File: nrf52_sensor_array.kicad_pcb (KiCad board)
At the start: 2 copper layers, 52.4 x 33.1 mm, 61 parts, among them J1 CONN_01X08, J2 CONN_01X08, J3 CONN_01X08, J4 CONN_01X08, J5 CONN_01X08, J6 CONN_01X08, P1 CONN_2, P2 CONN_2, P3 CONN_2, P4 CONN_2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

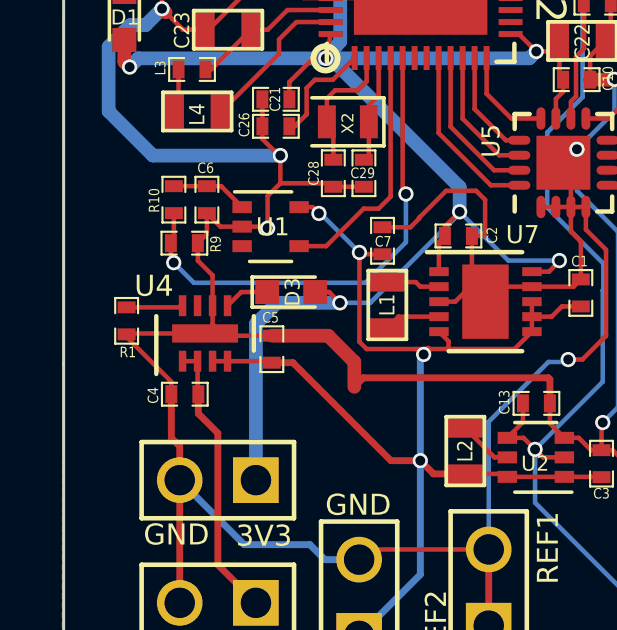
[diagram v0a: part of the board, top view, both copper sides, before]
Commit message: Placed corrected footprint.
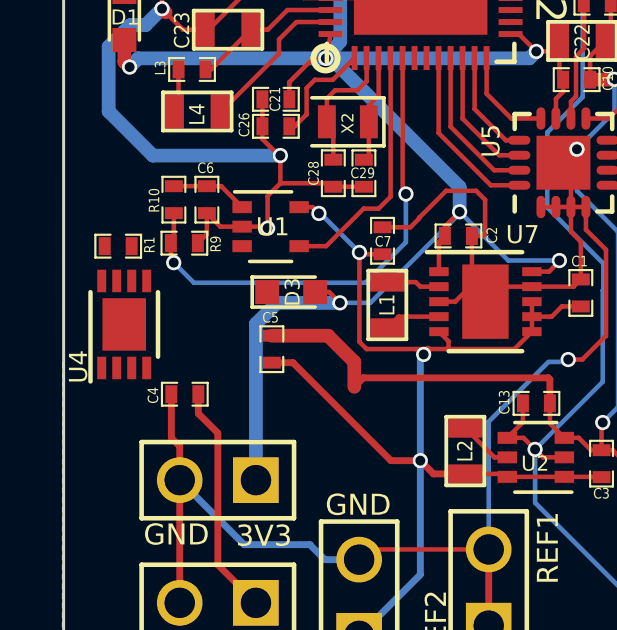
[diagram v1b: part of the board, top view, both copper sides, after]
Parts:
- U4: footprint Housings_DFN_QFN:DFN-8-1EP_2x3mm_Pitch0.5mm -> Housings_DFN_QFN:DFN-8-1EP_3x2mm_Pitch0.5mm
- moved U4 2.71 mm to (267.9, 145.9)
- moved R1 2.51 mm to (267.7, 143.3), turned to 180 degrees
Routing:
- net AVSS: track 254.0 -> 243.1 mm
- net VCC: track 41.3 -> 39.4 mm
- net Net-(R1-Pad2): track 1.92 -> 0.00 mm
- net 5V_in_charge: track 9.36 -> 7.79 mm
- net Net-(D3-Pad1): track 1.51 -> 0.00 mm

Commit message: (work in progress), missing ground connection on PCB, no load sharing circuit.
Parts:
- moved C4 1.10 mm to (270.2, 149.3)
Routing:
- net AVSS: track 243.1 -> 249.8 mm, vias 17 -> 18
- net VCC: track 39.4 -> 44.1 mm
- net Net-(D3-Pad1): track 0.00 -> 4.17 mm
- net 5V_in_charge: track 7.79 -> 11.4 mm
- net Net-(R1-Pad2): track 0.00 -> 1.20 mm
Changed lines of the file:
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@@
   (general
     (links 238)
-    (no_connects 13)
-    (area 265.849999 125.449999 318.320001 158.600001)
+    (no_connects 0)
+    (area 265.6476 122.157123 321.400001 159.215733)
     (thickness 1.6)
     (drawings 27)
-    (tracks 1155)
+    (tracks 1177)
     (zones 0)
     (modules 61)
@@
   )
   (setup
-    (last_trace_width 0.4572)
+    (last_trace_width 0.229)
     (user_trace_width 0.152)
     (user_trace_width 0.229)
@@
   )
   (module SM0402 (layer F.Cu)
-    (at 269.94 148.205)
+    (at 270.24 149.26)
     (attr smd)
     (fp_text reference C4 (at -1.05 0.04 90) (layer F.SilkS)
@@
   (segment (start 269.73042 137.38) (end 269.73042 138.64258) (width 0.152) (layer F.Cu) (net 8))
   (segment (start 269.73042 138.64258) (end 269.593 138.78) (width 0.152) (layer F.Cu) (net 8))
+  (segment (start 269.77 151.07) (end 269.77 149.28042) (width 0.152) (layer F.Cu) (net 9))
+  (segment (start 269.77 149.28042) (end 269.79042 149.26) (width 0.152) (layer F.Cu) (net 9))
+  (segment (start 273.125 140.25) (end 268.875 140.25) (width 0.152) (layer B.Cu) (net 9))
+  (via (at 268.875 140.25) (size 0.508) (drill 0.3302) (layers F.Cu B.Cu) (net 9))
+  (segment (start 268.16958 140.95542) (end 268.16958 143.27) (width 0.152) (layer F.Cu) (net 9))
+  (segment (start 268.875 140.25) (end 268.16958 140.95542) (width 0.152) (layer F.Cu) (net 9))
+  (segment (start 267.5575 146.3175) (end 268.2825 146.3175) (width 0.152) (layer F.Cu) (net 9))
+  (segment (start 267.5575 145.4425) (end 267.5575 146.3175) (width 0.152) (layer F.Cu) (net 9))
+  (segment (start 268.2825 145.4425) (end 267.5575 145.4425) (width 0.152) (layer F.Cu) (net 9))
+  (segment (start 268.17 144.43) (end 268.17 145.33) (width 0.152) (layer F.Cu) (net 9))
+  (segment (start 268.17 145.33) (end 268.2825 145.4425) (width 0.152) (layer F.Cu) (net 9))
+  (segment (start 268.17 144.43) (end 268.17 143.27042) (width 0.152) (layer F.Cu) (net 9))
+  (segment (start 268.17 143.27042) (end 268.16958 143.27) (width 0.152) (layer F.Cu) (net 9))
   (segment (start 288.06 151.12) (end 288.06 150.76) (width 0.152) (layer F.Cu) (net 9))
   (segment (start 287.63 148.83958) (end 287.87 148.59958) (width 0.152) (layer F.Cu) (net 9))
@@
   (segment (start 274.11 153.22) (end 271.92 153.22) (width 0.229) (layer B.Cu) (net 9))
   (segment (start 274.61 153.72) (end 274.11 153.22) (width 0.229) (layer B.Cu) (net 9))
-  (segment (start 269.49042 148.205) (end 269.49042 149.66042) (width 0.229) (layer F.Cu) (net 9))
-  (segment (start 269.77 149.94) (end 269.77 151.07) (width 0.229) (layer F.Cu) (net 9))
-  (segment (start 269.49042 149.66042) (end 269.77 149.94) (width 0.229) (layer F.Cu) (net 9))
   (segment (start 269.77 151.07) (end 269.77 155.16) (width 0.229) (layer F.Cu) (net 9))
   (segment (start 295.01958 130.01) (end 295.27 130.01) (width 0.152) (layer F.Cu) (net 9))
@@
   (via (at 269.18 135.355) (size 0.508) (drill 0.3302) (layers F.Cu B.Cu) (net 9))
   (via (at 273.125 140.25) (size 0.508) (drill 0.3302) (layers F.Cu B.Cu) (net 9))
-  (segment (start 268.875 140.25) (end 273.125 140.25) (width 0.4572) (layer B.Cu) (net 9))
   (segment (start 267.4 138.775) (end 268.875 140.25) (width 0.4572) (layer B.Cu) (net 9))
   (segment (start 267.4 136.625) (end 267.4 138.775) (width 0.4572) (layer B.Cu) (net 9))
@@
   (segment (start 294.12042 130.01) (end 292.85 130.01) (width 0.152) (layer F.Cu) (net 11))
   (segment (start 292.85 130.01) (end 292.81 129.97) (width 0.152) (layer F.Cu) (net 11))
+  (segment (start 268.67 147.33) (end 271.44 147.33) (width 0.152) (layer F.Cu) (net 12))
+  (segment (start 271.61542 147.15458) (end 272.84 147.15458) (width 0.152) (layer F.Cu) (net 12))
+  (segment (start 271.44 147.33) (end 271.61542 147.15458) (width 0.152) (layer F.Cu) (net 12))
+  (segment (start 268.17 147.33) (end 268.67 147.33) (width 0.152) (layer F.Cu) (net 12))
   (segment (start 277.79 150.42) (end 277.79 154.22) (width 0.229) (layer B.Cu) (net 12))
   (segment (start 277.79 154.22) (end 275.75 156.26) (width 0.229) (layer B.Cu) (net 12))
   (segment (start 272.84 147.15458) (end 273.54458 147.15458) (width 0.229) (layer F.Cu) (net 12))
-  (segment (start 276.81 150.42) (end 277.79 150.42) (width 0.229) (layer F.Cu) (net 12))
   (segment (start 273.54458 147.15458) (end 276.81 150.42) (width 0.229) (layer F.Cu) (net 12))
+  (segment (start 276.81 150.42) (end 277.79 150.42) (width 0.229) (layer F.Cu) (net 12))
   (segment (start 278.05 146.7) (end 278.05 146.73) (width 0.229) (layer F.Cu) (net 12))
   (segment (start 278.05 146.73) (end 277.9 146.88) (width 0.229) (layer F.Cu) (net 12))
@@
   (segment (start 271.15042 141.27042) (end 271.85 141.97) (width 0.152) (layer F.Cu) (net 39))
   (segment (start 270.675 141.27042) (end 269.575 141.27042) (width 0.152) (layer F.Cu) (net 39))
-  (segment (start 270.38958 148.205) (end 270.38958 148.84958) (width 0.229) (layer F.Cu) (net 40))
-  (segment (start 271.04 153.89) (end 272.31 155.16) (width 0.229) (layer F.Cu) (net 40))
-  (segment (start 271.04 149.5) (end 271.04 153.89) (width 0.229) (layer F.Cu) (net 40))
-  (segment (start 270.38958 148.84958) (end 271.04 149.5) (width 0.229) (layer F.Cu) (net 40))
-  (segment (start 270.365 148.18042) (end 270.38958 148.205) (width 0.152) (layer F.Cu) (net 40))
+  (segment (start 272.31 155.16) (end 272.31 154.61) (width 0.229) (layer F.Cu) (net 40))
+  (segment (start 272.31 154.61) (end 270.86 153.16) (width 0.229) (layer F.Cu) (net 40))
+  (segment (start 270.86 153.16) (end 270.86 149.43042) (width 0.229) (layer F.Cu) (net 40))
+  (segment (start 270.86 149.43042) (end 270.68958 149.26) (width 0.229) (layer F.Cu) (net 40))
+  (segment (start 267.67 147.33) (end 267.67 148.14) (width 0.152) (layer F.Cu) (net 40))
+  (segment (start 269.849825 148.420245) (end 270.68958 149.26) (width 0.152) (layer F.Cu) (net 40))
+  (segment (start 267.950245 148.420245) (end 269.849825 148.420245) (width 0.152) (layer F.Cu) (net 40))
+  (segment (start 267.67 148.14) (end 267.950245 148.420245) (width 0.152) (layer F.Cu) (net 40))
+  (segment (start 267.17 147.33) (end 267.67 147.33) (width 0.152) (layer F.Cu) (net 40))
+  (segment (start 267.17 144.43) (end 267.17 143.37042) (width 0.152) (layer F.Cu) (net 41))
+  (segment (start 267.17 143.37042) (end 267.27042 143.27) (width 0.152) (layer F.Cu) (net 41))
+  (segment (start 272.685 144.8) (end 270.2 144.8) (width 0.152) (layer F.Cu) (net 43))
+  (segment (start 269.83 144.43) (end 268.67 144.43) (width 0.152) (layer F.Cu) (net 43))
+  (segment (start 270.2 144.8) (end 269.83 144.43) (width 0.152) (layer F.Cu) (net 43))
   (segment (start 274.8 131.8) (end 274.15 131.8) (width 0.152) (layer F.Cu) (net 44))
   (segment (start 267.925 133.45) (end 267.925 134.8) (width 0.152) (layer F.Cu) (net 44))
@@
     (connect_pads (clearance 0.508))
     (min_thickness 0.254)
-    (fill (arc_segments 16) (thermal_gap 0.508) (thermal_bridge_width 0.508))
+    (fill yes (arc_segments 16) (thermal_gap 0.508) (thermal_bridge_width 0.508))
     (polygon
       (pts
@@
     (connect_pads (clearance 0.508))
     (min_thickness 0.254)
-    (fill (arc_segments 16) (thermal_gap 0.508) (thermal_bridge_width 0.508))
+    (fill yes (arc_segments 16) (thermal_gap 0.508) (thermal_bridge_width 0.508))
     (polygon
       (pts
